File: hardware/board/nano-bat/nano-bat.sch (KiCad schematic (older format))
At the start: 15 parts, among them J101 Barrel_Jack_Switch, J102 USB_B_Mini, J103 Screw_Terminal_01x02, J104 Conn_01x02, Q101 Q_PMOS_GSD

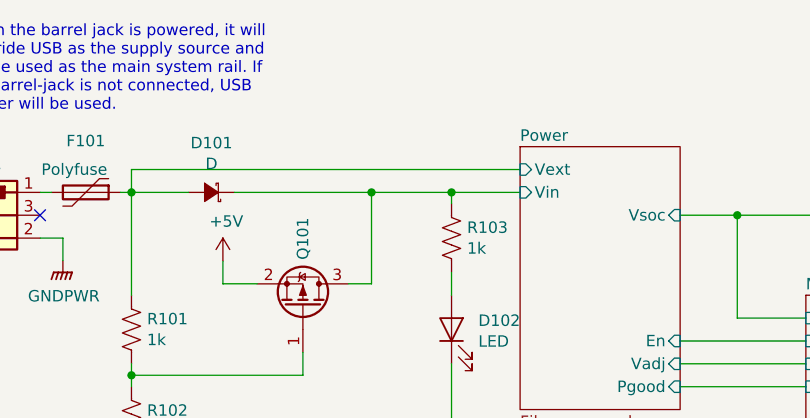
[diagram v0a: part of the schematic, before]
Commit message: Adding test points, initial board outline
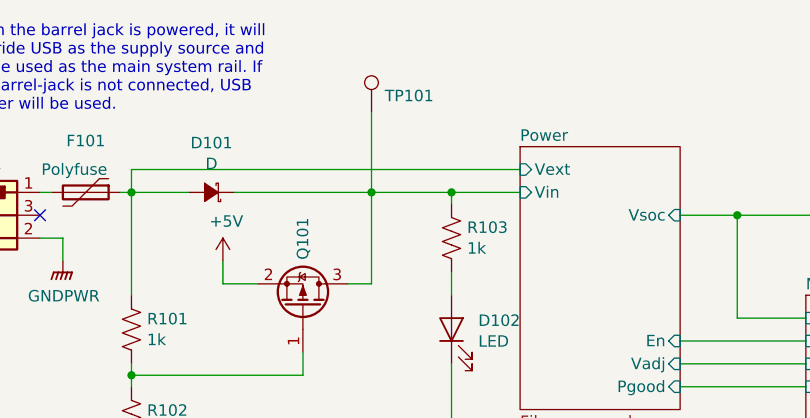
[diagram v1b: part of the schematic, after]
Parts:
- added TP101: TestPoint, TestPoint:TestPoint_Plated_Hole_D2.0mm, symbol Connector:TestPoint
- J102: footprint footprints:USB-MICRO-B-HIROSE-UX60-MB-5S8 -> Connector_USB:USB_Mini-B_Lumberg_2486_01_Horizontal; Part H2960CT-ND -> 609-4701-1-ND
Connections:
- net Power/Vin: now also TP101.1
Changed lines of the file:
@@
 F 0 "J102" H 3507 5067 50  0000 C CNN
 F 1 "USB_B_Mini" H 3507 4976 50  0000 C CNN
-F 2 "footprints:USB-MICRO-B-HIROSE-UX60-MB-5S8" H 3600 4550 50  0001 C CNN
+F 2 "Connector_USB:USB_Mini-B_Lumberg_2486_01_Horizontal" H 3600 4550 50  0001 C CNN
 F 3 "~" H 3600 4550 50  0001 C CNN
-F 4 "H2960CT-ND" H 3450 4600 50  0001 C CNN "Part"
+F 4 "609-4701-1-ND" H 3450 4600 50  0001 C CNN "Part"
 	1    3450 4600
 	1    0    0    -1
@@
 Text Notes 1350 2250 0    50   ~ 0
 When the barrel jack is powered, it will \noverride USB as the supply source and \nwill be used as the main system rail. If \nthe barrel-jack is not connected, USB\n power will be used.
+$Comp
+L Connector:TestPoint TP101
+U 1 1 5E31A2AF
+P 3150 2250
+F 0 "TP101" H 3208 2322 50  0000 L CNN
+F 1 "TestPoint" H 3208 2277 50  0001 L CNN
+F 2 "TestPoint:TestPoint_Plated_Hole_D2.0mm" H 3350 2250 50  0001 C CNN
+F 3 "~" H 3350 2250 50  0001 C CNN
+	1    3150 2250
+	1    0    0    -1
+$EndComp
+Wire Wire Line
+	3150 2250 3150 2600
 $EndSCHEMATC
